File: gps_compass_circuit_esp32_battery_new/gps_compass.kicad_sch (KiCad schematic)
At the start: 58 parts, among them J1 USB_C_Receptacle_PowerOnly_6P, Q1 MMBTA92, U1 MCP1700x-330xxTT, U3 LTC4054ES5-4.2

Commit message: Aggiornamenti vari
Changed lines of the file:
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@@
   (symbol (lib_id "Connector:Conn_01x03_Socket") (at 269.24 54.61 0) (mirror x) (unit 1)
     (in_bom yes) (on_board yes) (dnp no)
-    (property "Reference" "Serial1" (at 270.51 55.88 0)
+    (property "Reference" "Serial1" (at 271.78 50.8 90)
       (effects (font (size 1.27 1.27)) (justify left))
     )
-    (property "Value" "Conn_01x03_Socket" (at 270.51 53.34 0)
+    (property "Value" "Conn_01x03_Socket" (at 274.32 50.8 90)
       (effects (font (size 1.27 1.27)) (justify left))
     )

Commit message: Aggiunto led rgb seriale
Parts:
- removed LED1: LED, LED_THT:LED_D3.0mm, symbol Device:LED
- removed R6: R, Resistor_SMD:R_0603_1608Metric_Pad0.98x0.95mm_HandSolder, symbol Device:R
- added C12: 0,1uF, Capacitor_SMD:C_0603_1608Metric_Pad1.08x0.95mm_HandSolder, symbol Device:C
- added C13: 1uF, Capacitor_SMD:C_0603_1608Metric_Pad1.08x0.95mm_HandSolder, symbol Device:C
- added D3: WS2812B, LED_SMD:LED_WS2812B_PLCC4_5.0x5.0mm_P3.2mm, symbol LED:WS2812B
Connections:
- net GND: now also C12.2, C13.2, D3.3 (VSS)
- net VCC: now also C12.1, C13.1, D3.1 (VDD)
- net at ESP32-S1.8 (IO32): now also D3.4 (DIN)
- no-connect marks 18 -> 19

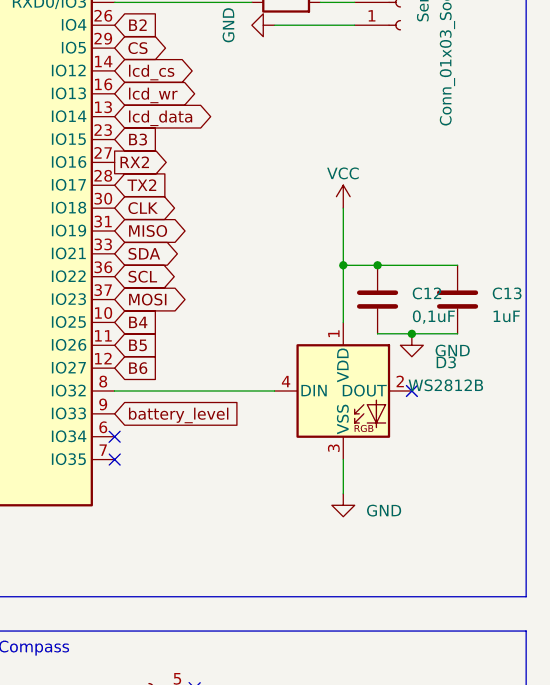
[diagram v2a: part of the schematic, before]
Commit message: Riprestinato led non rgb
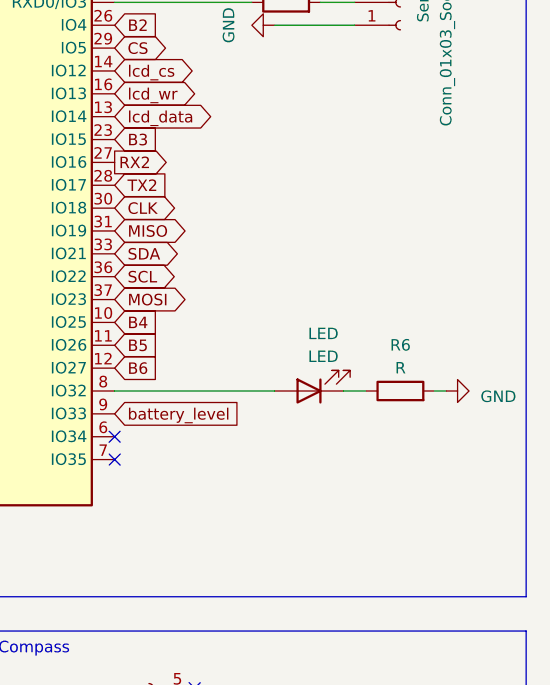
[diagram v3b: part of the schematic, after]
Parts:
- removed C12: 0,1uF, Capacitor_SMD:C_0603_1608Metric_Pad1.08x0.95mm_HandSolder, symbol Device:C
- removed C13: 1uF, Capacitor_SMD:C_0603_1608Metric_Pad1.08x0.95mm_HandSolder, symbol Device:C
- removed D3: WS2812B, LED_SMD:LED_WS2812B_PLCC4_5.0x5.0mm_P3.2mm, symbol LED:WS2812B
- added LED: LED, LED_THT:LED_D3.0mm, symbol Device:LED
- added R6: R, Resistor_SMD:R_0603_1608Metric_Pad0.98x0.95mm_HandSolder, symbol Device:R
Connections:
- net GND: now also R6.2
- net at ESP32-S1.8 (IO32): now also LED.2 (A)
- new net: LED.1 (K), R6.1
- no-connect marks 19 -> 18
